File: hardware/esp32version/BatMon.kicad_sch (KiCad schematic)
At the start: 30 parts, among them J1 Battery_Connector, J2 Charging_Connector, J3 Prog_Connector, J4 RESET, Q1 Q_PMOS_DDGSDD_TSOP-6, Q2 Q_PMOS_DDGSDD_TSOP-6, Q3 SS8050-G, U1 ESP32-WROOM-32D, U2 LM2904, U3 AMS1117

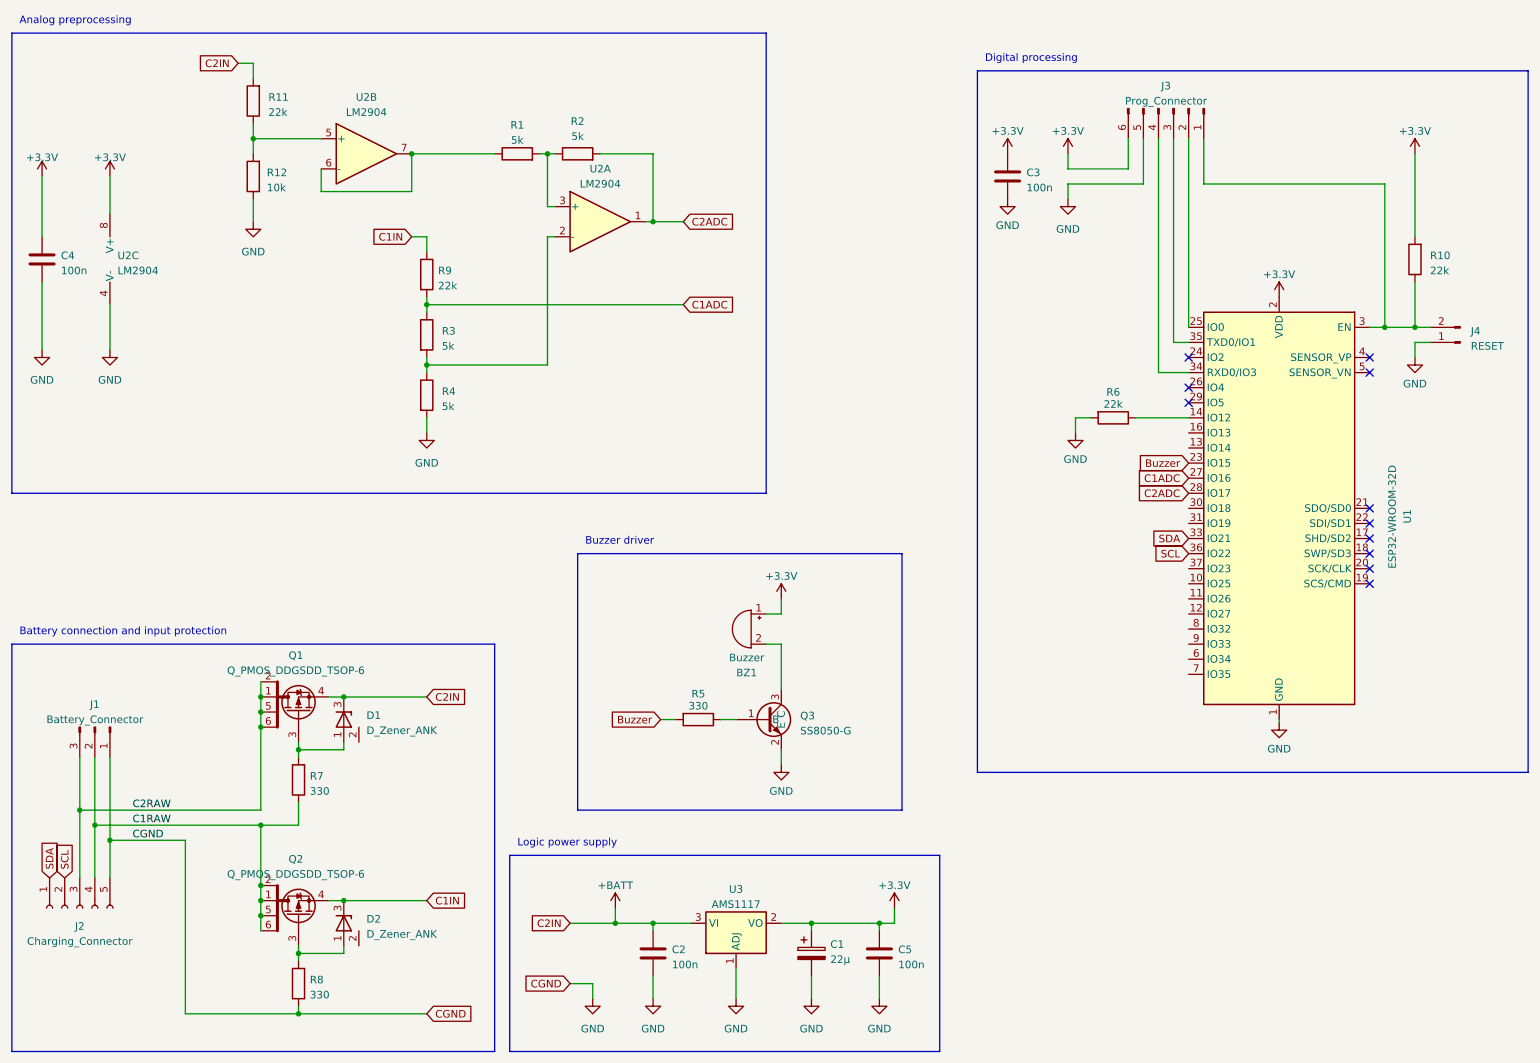
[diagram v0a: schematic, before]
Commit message: implemented new analog section, started component selection process
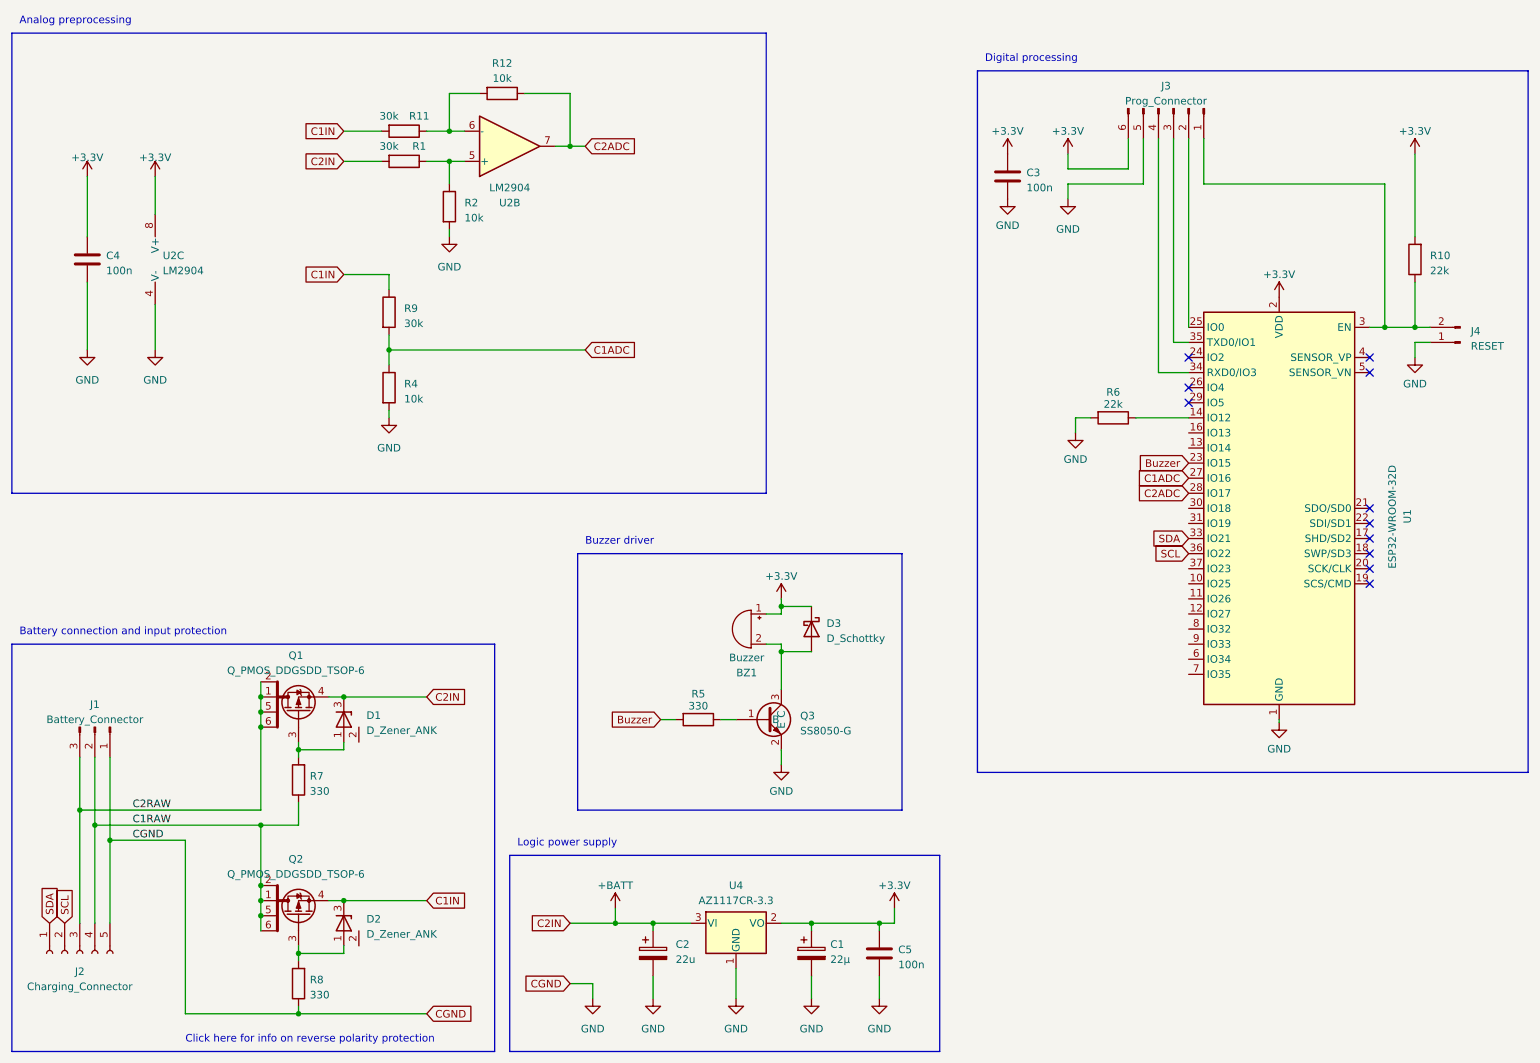
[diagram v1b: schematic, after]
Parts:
- removed C2: 100n, Capacitor_SMD:C_0603_1608Metric_Pad1.08x0.95mm_HandSolder, symbol Device:C
- removed R3: 5k, Resistor_SMD:R_0603_1608Metric_Pad0.98x0.95mm_HandSolder, symbol Device:R
- removed unit 1 of U2
- removed U3: AMS1117, Package_TO_SOT_SMD:SOT-223-3_TabPin2, symbol Regulator_Linear:AMS1117
- added C2: 22u, Capacitor_Tantalum_SMD:CP_EIA-3216-18_Kemet-A_Pad1.58x1.35mm_HandSolder, symbol Device:C_Polarized
- added D3: D_Schottky, Diode_SMD:D_SOD-123, symbol Device:D_Schottky
- added U4: AZ1117CR-3.3, Package_TO_SOT_SMD:SOT-89-3_Handsoldering, symbol Regulator_Linear:AZ1117-3.3
- BZ1: Mouser (none) -> https://www.mouser.at/ProductDetail/CUI-Devices/CMT-85853-9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
- C1: footprint Capacitor_SMD:C_0603_1608Metric_Pad1.08x0.95mm_HandSolder -> Capacitor_Tantalum_SMD:CP_EIA-3216-18_Kemet-A_Pad1.58x1.35mm_HandSolder; Mouser (none) -> https://www.mouser.at/ProductDetail/KEMET/T491A226K010AT?qs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
- Q1, Q2: Mouser (none) -> https://www.mouser.at/ProductDetail/Vishay-Siliconix/SI3483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
- Q3: Mouser (none) -> https://www.mouser.at/ProductDetail/Comchip-Technology/SS80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
- R1: value 5k -> 30k
- R11, R9: value 22k -> 30k
- R2, R4: value 5k -> 10k
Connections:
- net +3.3V: now also D3.1 (K), U4.2 (VO)
- net +BATT: now also R1.2, C2.1, U4.3 (VI); no longer R11.2
- net C1ADC: now also R4.1
- net C1IN: now also R11.2
- net C2ADC: now also R12.1, U2.7; no longer R2.2
- net GND: now also R2.2, C2.2, U4.1 (GND); no longer R12.1
- net at R11.1, R12.2: now also U2.6 (-); no longer U2.5 (+)
- net at R2.1: now also R1.1, U2.5 (+); no longer R1.2
- net at BZ1.2 (+), Q3.3 (C): now also D3.2 (A)
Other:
- note added: "Click here for info on reverse polarity protection"
- moved on the sheet: C4, J2, R11, R12, U2B, U2C

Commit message: worked on schematic and part selection
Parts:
- added D4: LED, symbol Device:LED
- added R3: R, symbol Device:R
- BZ1: Mouser https://www.mouser.at/ProductDetail/CUI-Devices/CMT-85853-9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 -> (none)
- C1: Mouser https://www.mouser.at/ProductDetail/KEMET/T491A226K010AT?qs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 -> (none)
- C2: value 22u -> 22µ; Mouser https://www.mouser.at/ProductDetail/KEMET/T491A226K010AT?qs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 -> (none)
- D1, D2: Mouser https://www.mouser.at/ProductDetail/Vishay-Semiconductors/M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 -> (none)
- D3: Mouser https://www.mouser.at/ProductDetail/Nexperia/PMEG4030ETRX?q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 -> (none)
- J1: footprint Connector_PinHeader_2.54mm:PinHeader_1x03_P2.54mm_Horizontal -> Connector_JST:JST_XH_S3B-XH-A_1x03_P2.50mm_Horizontal
- J2: Receptacle (none) -> https://www.mouser.at/ProductDetail/TE-Connectivity-AMP/3-8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
- Q1, Q2: Mouser https://www.mouser.at/ProductDetail/Vishay-Siliconix/SI3483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 -> (none)
- Q3: Mouser https://www.mouser.at/ProductDetail/Comchip-Technology/SS80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 -> (none)
- U1: Mouser https://www.mouser.at/ProductDetail/Espressif-Systems/ESP32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 -> (none)
- U2: Mouser https://www.mouser.at/ProductDetail/Texas-Instruments/LM290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 -> (none)
- U4: Mouser https://www.mouser.at/ProductDetail/Diodes-Incorporated/AZ1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 -> (none)
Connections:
- net GND: now also D4.1 (K)
- net at U1.11 (IO26): now also R3.2
- new net: D4.2 (A), R3.1

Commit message: started working on new layout
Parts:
- removed J2: Charging_Connector, Connector_PinHeader_2.54mm:PinHeader_1x05_P2.54mm_Horizontal, symbol Connector:Conn_01x05_Socket
- removed J4: RESET, Connector_PinHeader_2.54mm:PinHeader_1x02_P2.54mm_Vertical, symbol Connector:Conn_01x02_Pin
- added D5: ~, ELEKTRON_Footprints:D_TVS_Quad_Array_1206, symbol ELEKTRON_Components:D_TVS_Quad_Array
- added J5: Charging_Connector, ELEKTRON_Footprints:Conn_Edge_1x6_LLSSSS_Mirrored, symbol Connector_Generic:Conn_01x06
- added unit 1 of U2
- D4: footprint (none) -> LED_SMD:LED_0603_1608Metric_Pad1.05x0.95mm_HandSolder
- J3: footprint Connector_PinHeader_2.54mm:PinHeader_1x06_P2.54mm_Vertical -> ELEKTRON_Footprints:Dbg_Port_1x6_P1.27mm_ThroughHole; Note (none) -> This is just an empty row of through holes where the progra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; now not fitted
- R3: footprint (none) -> Resistor_SMD:R_0603_1608Metric_Pad0.98x0.95mm_HandSolder
- R9: value 30k -> 20k
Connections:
- net C1RAW is gone; now on net GND: J1.2 (Pin_2), Q2.1 (D), Q2.2 (D), Q2.5 (D), Q2.6 (D), R7.1
- net C2RAW is gone; now on net GND: J1.3 (Pin_3), Q1.1 (D), Q1.2 (D), Q1.5 (D), Q1.6 (D)
- net +3.3V: now also J5.2 (Pin_2)
- net GND: now also D5.3 (A1), D5.4 (A1), D5.5 (A2), D5.6 (A2), D5.7 (A2), D5.8 (A2), J5.1 (Pin_1), J5.5 (Pin_5), J5.6 (Pin_6)
- net SCL: now also D5.2 (A1), J5.4 (Pin_4)
- net SDA: now also D5.1 (A1), J5.3 (Pin_3)
- no-connect marks 11 -> 14
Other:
- moved on the sheet: BZ1, C1, C2, C3, C4, C5, D1, D2, D3, J1, Q1, Q2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

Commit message: first iteration of new pcb done
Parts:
- added D6: D_Zener, Diode_SMD:D_0603_1608Metric_Pad1.05x0.95mm_HandSolder, symbol Device:D_Zener
- D1, D2: footprint Package_TO_SOT_SMD:TSOT-23_HandSoldering -> Package_TO_SOT_SMD:TSOT-23
- R10, R6: value 22k -> 10k
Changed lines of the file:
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@@
+    )
+  )
+  (symbol (lib_id "Device:D_Zener") (at 87.63 127 270) (unit 1)
+    (in_bom yes) (on_board no) (dnp no) (fields_autoplaced)
+    (property "Reference" "D6" (at 90.17 126.365 90)
+      (effects (font (size 1.27 1.27)) (justify left))
+    )
+    (property "Value" "D_Zener" (at 90.17 128.905 90)
+      (effects (font (size 1.27 1.27)) (justify left))
+    )
+    (property "Footprint" "Diode_SMD:D_0603_1608Metric_Pad1.05x0.95mm_HandSolder" (at 87.63 127 0)
+      (effects (font (size 1.27 1.27)) hide)
+    )
+    (property "Datasheet" "https://www.mouser.at/ProductDetail/Taiwan-Semiconductor/TSZU52C4V3-RGG?qs=QEzMiVqgwc3BSs82ijdejg%3D%3D" (at 87.63 127 0)
+      (effects (font (size 1.27 1.27)) hide)
+    )
+    (pin "1")
+    (pin "2")
+    (instances
+      (project "BatMon"
+        (path "/8cdf4f9d-1967-4f03-a23a-bb9e47281b6b"
+          (reference "D6") (unit 1)
+        )
+      )
     )
   )
@@
       (effects (font (size 1.27 1.27)) (justify right))
     )
-    (property "Value" "22k" (at 257.81 59.055 0)
+    (property "Value" "10k" (at 257.81 59.055 0)
       (effects (font (size 1.27 1.27)) (justify right))
     )
@@
       (effects (font (size 1.27 1.27)) (justify left))
     )
-    (property "Footprint" "Package_TO_SOT_SMD:TSOT-23_HandSoldering" (at 80.01 116.84 0)
+    (property "Footprint" "Package_TO_SOT_SMD:TSOT-23" (at 80.01 116.84 0)
       (effects (font (size 1.27 1.27)) hide)
     )
@@
       (effects (font (size 1.27 1.27)))
     )
-    (property "Value" "22k" (at 204.47 81.534 90)
+    (property "Value" "10k" (at 204.47 81.534 90)
       (effects (font (size 1.27 1.27)))
     )
@@
       (effects (font (size 1.27 1.27)) (justify left))
     )
-    (property "Footprint" "Package_TO_SOT_SMD:TSOT-23_HandSoldering" (at 80.01 151.13 0)
-      (effects (font (size 1.27 1.27)) hide)
-    )
+    (property "Footprint" "Package_TO_SOT_SMD:TSOT-23" (at 80.01 151.13 0)
+      (effects (font (size 1.27 1.27)) hide)
+    )

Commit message: minor changes, round corners
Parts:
- removed D6: D_Zener, Diode_SMD:D_0603_1608Metric_Pad1.05x0.95mm_HandSolder, symbol Device:D_Zener
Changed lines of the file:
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@@
-    )
-  )
-  (symbol (lib_id "Device:D_Zener") (at 87.63 127 270) (unit 1)
-    (in_bom yes) (on_board no) (dnp no) (fields_autoplaced)
-    (property "Reference" "D6" (at 90.17 126.365 90)
-      (effects (font (size 1.27 1.27)) (justify left))
-    )
-    (property "Value" "D_Zener" (at 90.17 128.905 90)
-      (effects (font (size 1.27 1.27)) (justify left))
-    )
-    (property "Footprint" "Diode_SMD:D_0603_1608Metric_Pad1.05x0.95mm_HandSolder" (at 87.63 127 0)
-      (effects (font (size 1.27 1.27)) hide)
-    )
-    (property "Datasheet" "https://www.mouser.at/ProductDetail/Taiwan-Semiconductor/TSZU52C4V3-RGG?qs=QEzMiVqgwc3BSs82ijdejg%3D%3D" (at 87.63 127 0)
-      (effects (font (size 1.27 1.27)) hide)
-    )
-    (pin "1")
-    (pin "2")
-    (instances
-      (project "BatMon"
-        (path "/8cdf4f9d-1967-4f03-a23a-bb9e47281b6b"
-          (reference "D6") (unit 1)
-        )
-      )
     )
   )

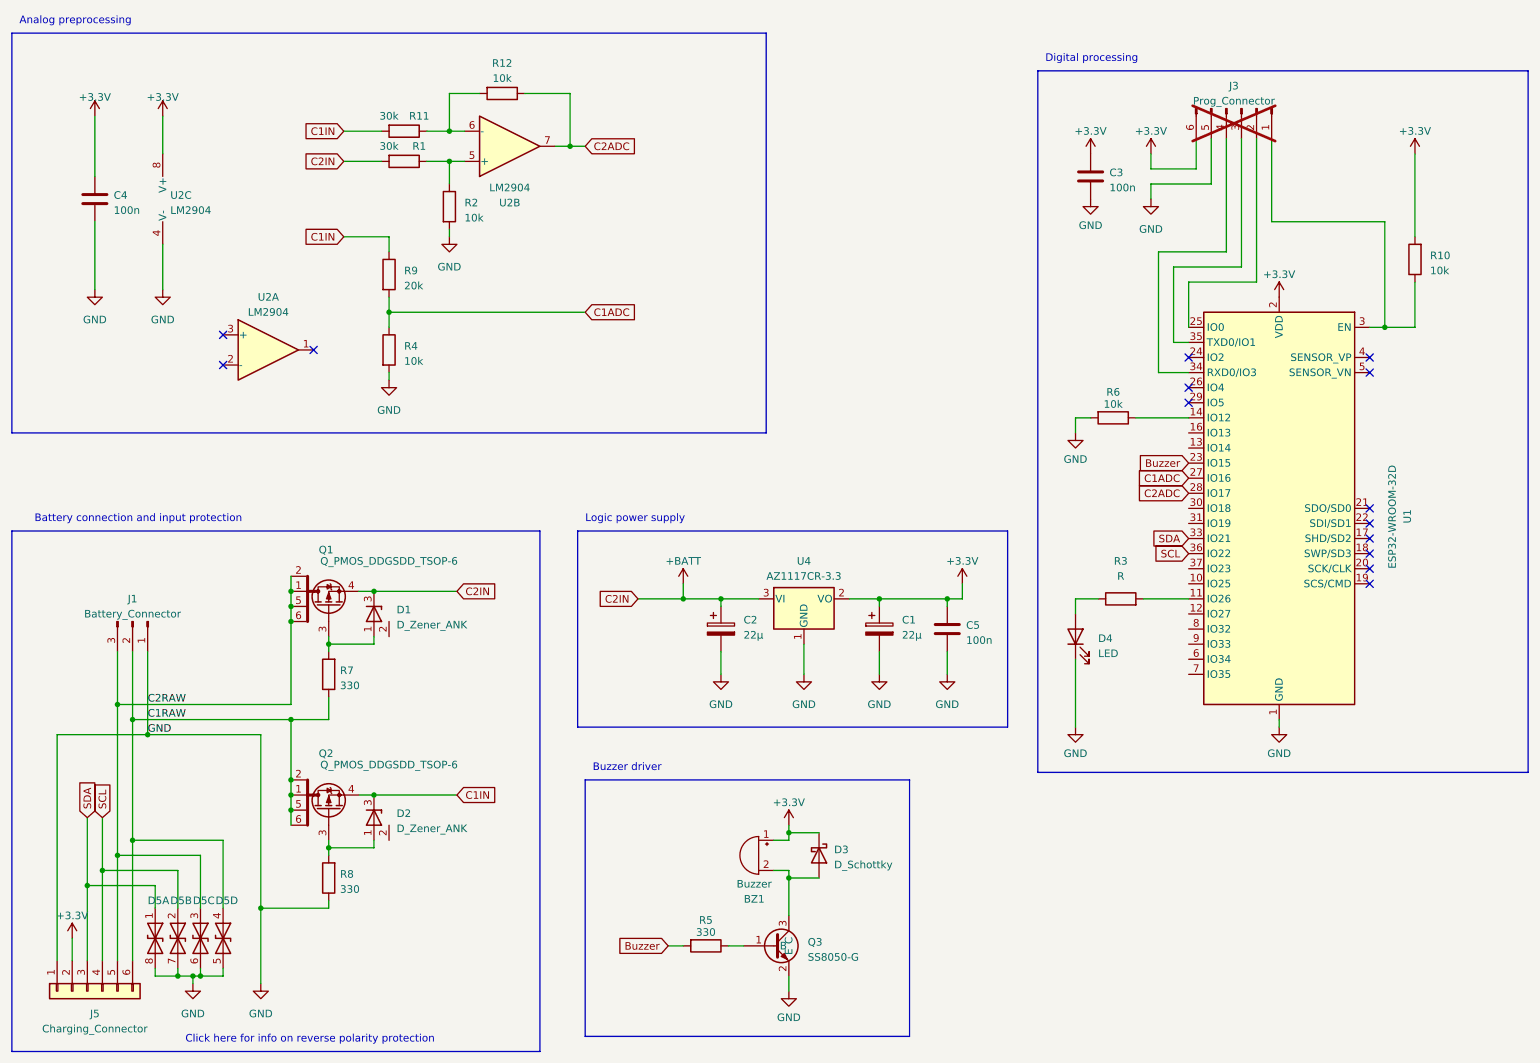
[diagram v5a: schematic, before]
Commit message: added a switch and fixed the battery pinout
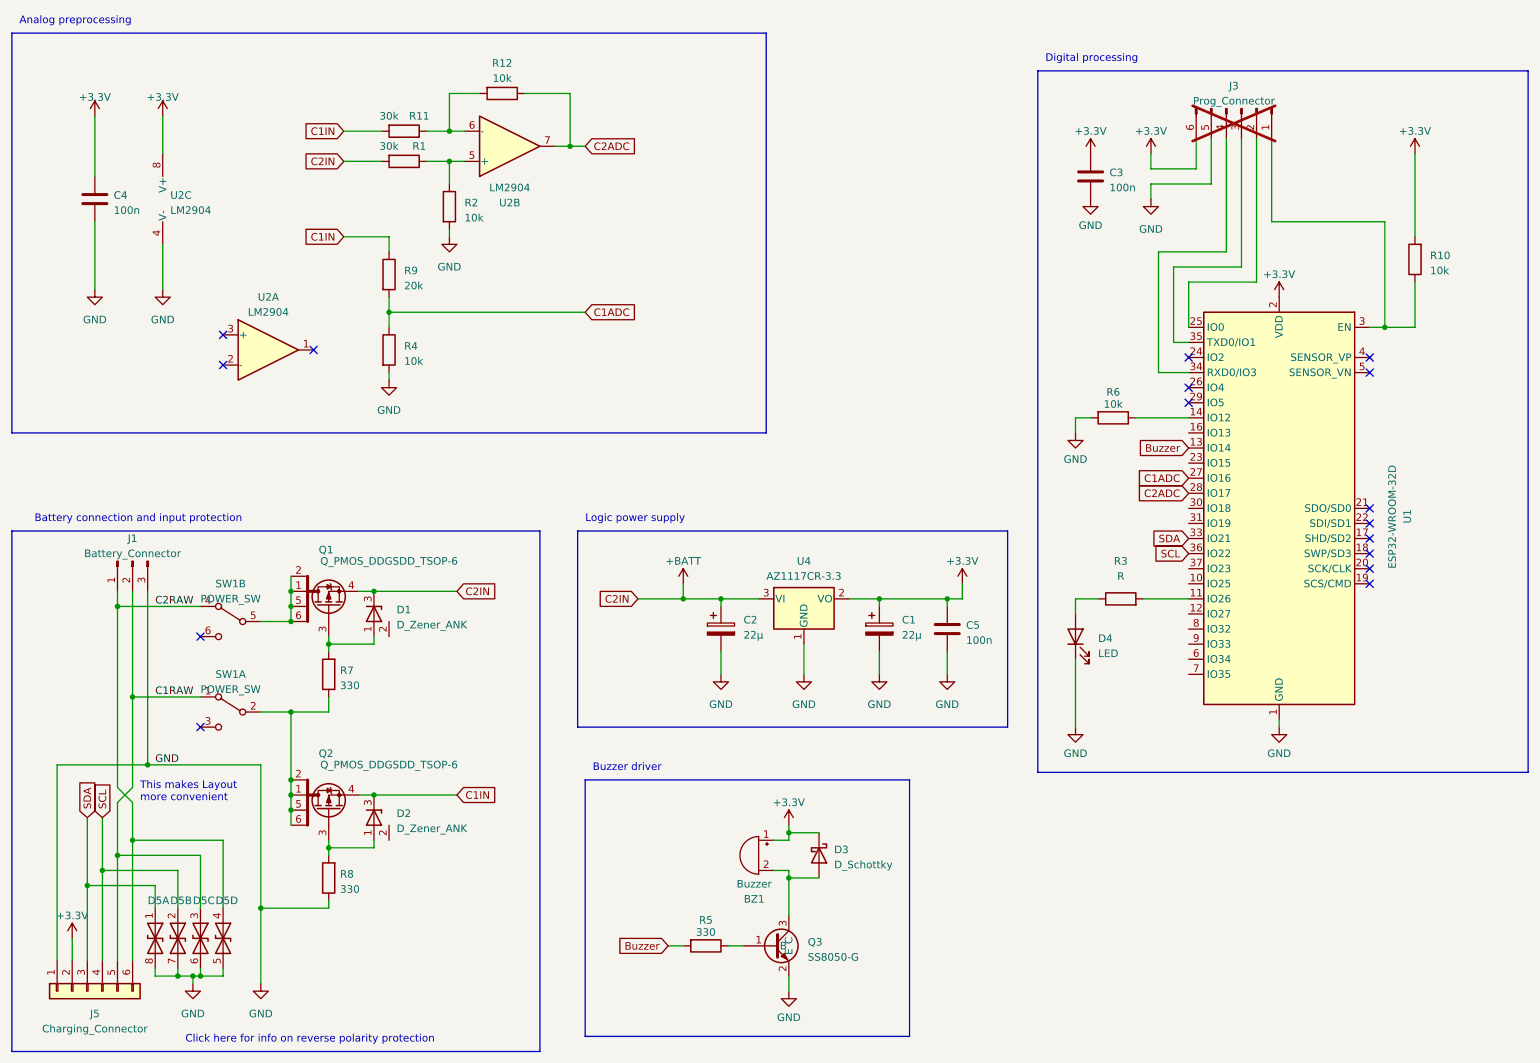
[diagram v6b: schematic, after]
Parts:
- added SW1: POWER_SW, ELEKTRON_Footprints:SW_DPDT_Nidec_CL-SB-22A-1x, symbol Switch:SW_DPDT_x2
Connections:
- net Buzzer: now also U1.13 (IO14); no longer U1.23 (IO15)
- net GND: no longer D5.3 (A1), D5.4 (A1), J1.1 (Pin_1), J1.2 (Pin_2), J5.5 (Pin_5), J5.6 (Pin_6), Q1.1 (D), Q1.2 (D), Q1.5 (D), Q1.6 (D), Q2.1 (D), Q2.2 (D), Q2.5 (D), Q2.6 (D), R7.1
- new net: Q1.1 (D), Q1.2 (D), Q1.5 (D), Q1.6 (D), SW1.5 (B)
- new net: Q2.1 (D), Q2.2 (D), Q2.5 (D), Q2.6 (D), R7.1, SW1.2 (B)
- new net C1RAW: D5.3 (A1), J1.2 (Pin_2), J5.5 (Pin_5), SW1.1 (A)
- new net C2RAW: D5.4 (A1), J1.1 (Pin_1), J5.6 (Pin_6), SW1.4 (A)
- no-connect marks 14 -> 16
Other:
- note added: "This makes Layout more convenient"
- moved on the sheet: J1
